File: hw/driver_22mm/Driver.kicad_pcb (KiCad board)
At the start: 4 copper layers, 22 x 22 mm, 50 parts, among them J1 +LED, J10 R, J11 G, J12 Button, J13 Button_GND, J2 -LED, J3 Button LED, J4 Button LED GND, J5 SWDIO, J6 SWCLK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

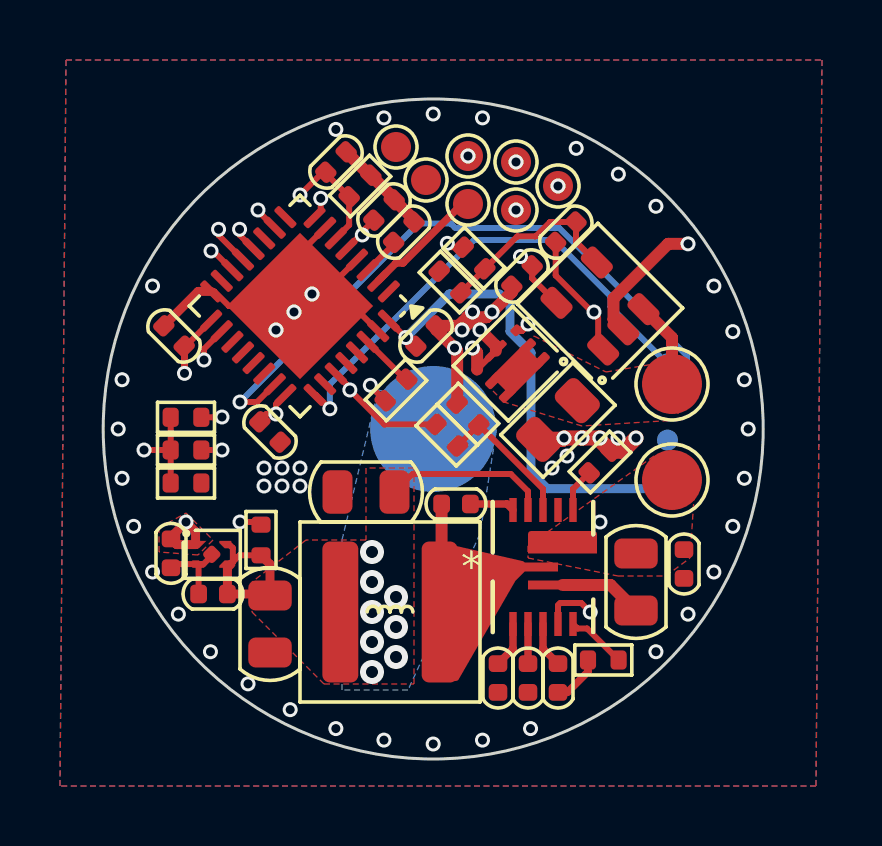
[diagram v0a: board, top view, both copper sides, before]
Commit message: Driver v2 changes
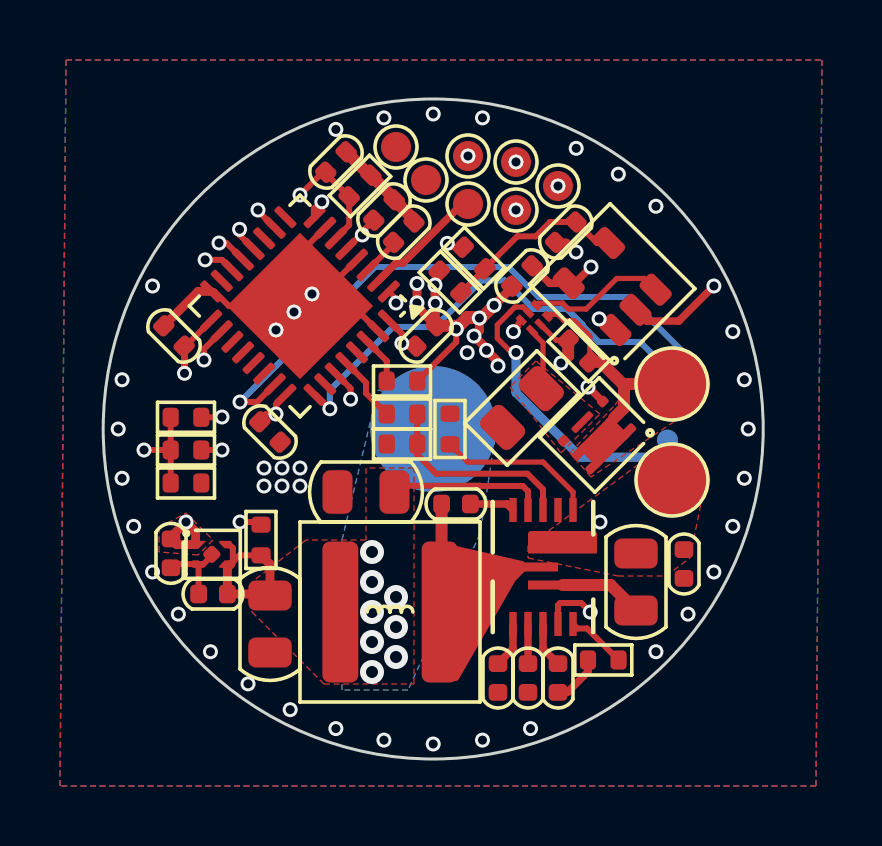
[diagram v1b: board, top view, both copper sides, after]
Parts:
- added R5: 7m - R_SENSE_MAIN, Resistor_SMD_AKL:R_0805_2012Metric, F.Cu at (94.4, 88.2)
- added U5: XS3A1T3157GSH, footprints:XSON6_SOT1202_NEX, F.Cu at (94.8, 85.2)
- Q1: value 7m - R_SENSE_MAIN -> ~
- R13: value 2.25M - R_BAT_TOP -> 1.6M - R_BAT_TOP
- R3: value 254k - R_DAC_TOP -> 285k - R_DAC_TOP
- R6: footprint Resistor_SMD_AKL:R_0805_2012Metric -> Resistor_SMD_AKL:R_0402_1005Metric
- U4: value NCP114AMX250TCG -> NCP114AMX280TCG
- moved R7 5.12 mm to (92.0, 88.9), turned to 90 degrees
- moved Q1 3.74 mm to (96.9, 89.1)
- moved R2 2.42 mm to (90.4, 89.4), turned to 180 degrees
- moved R6 2.40 mm to (96.3, 86.3), turned to 135 degrees
- moved R1 1.65 mm to (90.4, 88.4), turned to 0 degrees
- moved U2 0.77 mm to (97.4, 84.1)
- moved R12 0.36 mm to (90.4, 87.3), turned to 0 degrees
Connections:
- C8 pad 2: /EN -> /OPAMP_EN
- Q1 pad 4: GND -> Net-(Q1-S)
- R1 pad 1: /EN -> /BOOST_EN
- U2 pad 3: /-LED -> Net-(U2-+)
- U2 pad 5: /EN -> /OPAMP_EN
- U3 pad 1: unconnected-(U3-PC14-Pad1) -> /SHUNT_SELECT
- U3 pad 27: /EN -> /OPAMP_EN
- U3 pad 28: unconnected-(U3-PB6-Pad28) -> /BOOST_EN
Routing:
- net /OPAMP_EN: track 0.00 -> 15.1 mm, vias 0 -> 2
- net /EN: track 14.1 -> 0.00 mm, vias 2 -> 0
- net /SHUNT_SELECT: track 0.00 -> 7.27 mm, vias 0 -> 2
- net Net-(U2-+): track 0.00 -> 4.57 mm
- net /-LED: track 2.89 -> 6.91 mm
- net Net-(U1-ILIM): track 1.46 -> 5.36 mm
- net /HDR: track 10.5 -> 14.0 mm
- net /BOOST_EN: track 0.00 -> 2.26 mm
- net Net-(Q1-S): track 0.00 -> 2.20 mm
- net Net-(U1-EN): track 4.73 -> 6.72 mm
- net GND: track 43.3 -> 41.6 mm, vias 55 -> 52
- net /DAC: track 10.6 -> 8.86 mm
- net Net-(C7-Pad2): track 19.1 -> 20.6 mm, vias 2 -> 3
- net /SWCLK: track 16.7 -> 15.3 mm
- net /SWDIO: track 22.4 -> 21.2 mm
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- added copper zone on F.Cu, net Net-(Q1-S)
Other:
- board text added: "Boost driver Rev 1 Ben Simms Quak"
- board text removed: "Boost driver Rev 0 Ben Simms Croak"

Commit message: Stuff
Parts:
- removed J13: Button_GND, TestPoint:TestPoint_Pad_D1.0mm
- J4: value Button LED GND -> Wire GND; footprint TestPoint:TestPoint_Pad_D1.0mm -> TestPoint:TestPoint_Pad_D1.0mm_copy
- R11: value 450k - R_FB_C -> 434k - R_FB_C
- R5: value 7m - R_SENSE_MAIN -> 10m - R_SENSE_MAIN
- moved J4 0.54 mm to (90.7, 79.7), turned to -45 degrees
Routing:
- net GND: track 41.6 -> 43.0 mm
- net Net-(C7-Pad2): track 20.6 -> 21.3 mm
- net VCC: track 47.9 -> 48.5 mm

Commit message: Stuff
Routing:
- net VCC: track 48.5 -> 49.8 mm
- net GND: vias 52 -> 53
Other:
- board text added: "Boost driver Rev 2 Ben Simms Quak"
- board text removed: "Boost driver Rev 1 Ben Simms Quak"

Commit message: Push changes
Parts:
- moved U4 0.97 mm to (84.9, 92.6)
- moved C20 0.81 mm to (83.5, 92.9)
- moved R13 0.81 mm to (86.5, 92.7)
- moved C21 0.57 mm to (88.6, 80.4)
- moved R14 0.42 mm to (89.3, 81.1)
- moved C16 0.40 mm to (84.5, 94.4), turned to -90 degrees
- moved C10 0.30 mm to (99.8, 93.1)
- moved C14 0.29 mm to (90.7, 82.5)
- moved C18 0.28 mm to (90.0, 81.8)
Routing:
- net /BAT_SENSE: track 21.9 -> 23.3 mm
- net GND: track 43.0 -> 41.8 mm
- net +BATT: track 11.0 -> 10.3 mm
- net VCC: track 49.8 -> 49.1 mm
- removed copper zone on F.Cu, net VCC
